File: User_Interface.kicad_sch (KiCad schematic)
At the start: 24 parts, among them SW1 SPST-NO, SW2 SPST-NO, U11 74LVC1G38, U12 74LVC1G38, U13 74LVC1G38

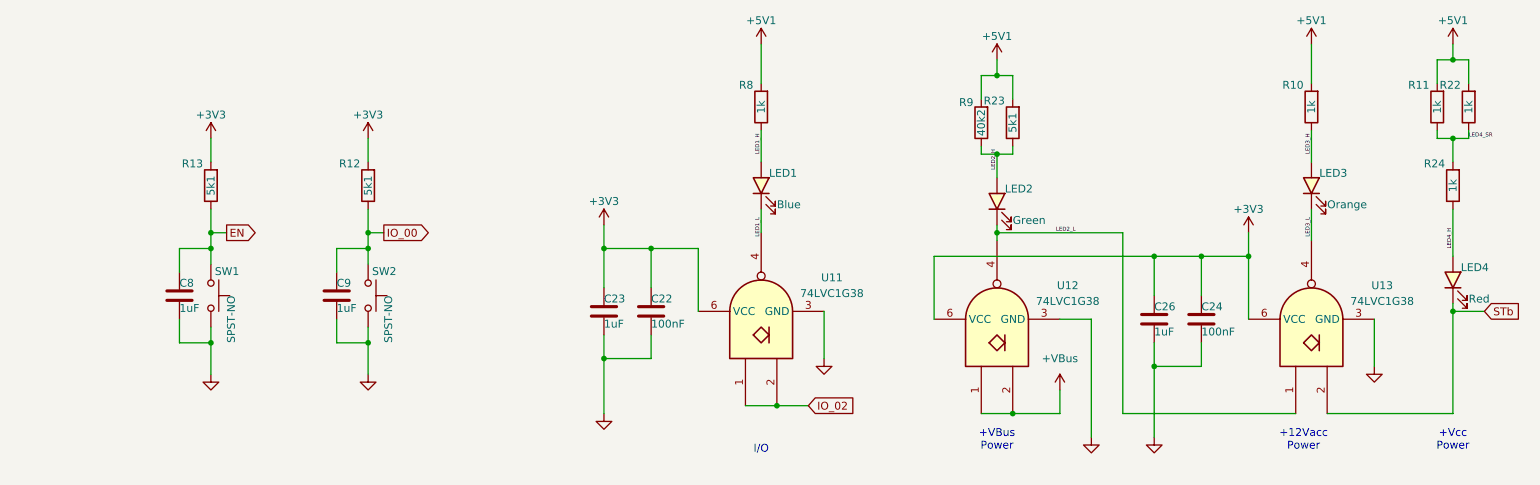
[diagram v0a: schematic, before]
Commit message: streamlined routing by discarding legacy GPIO pinout compatibility. reduced Vin to Vcc and Vbus (no more +16V) includes CAN & Vehicle inputs (need to move to 2nd board, though) added wake-on-start by wiring Vacc to RTC_IO
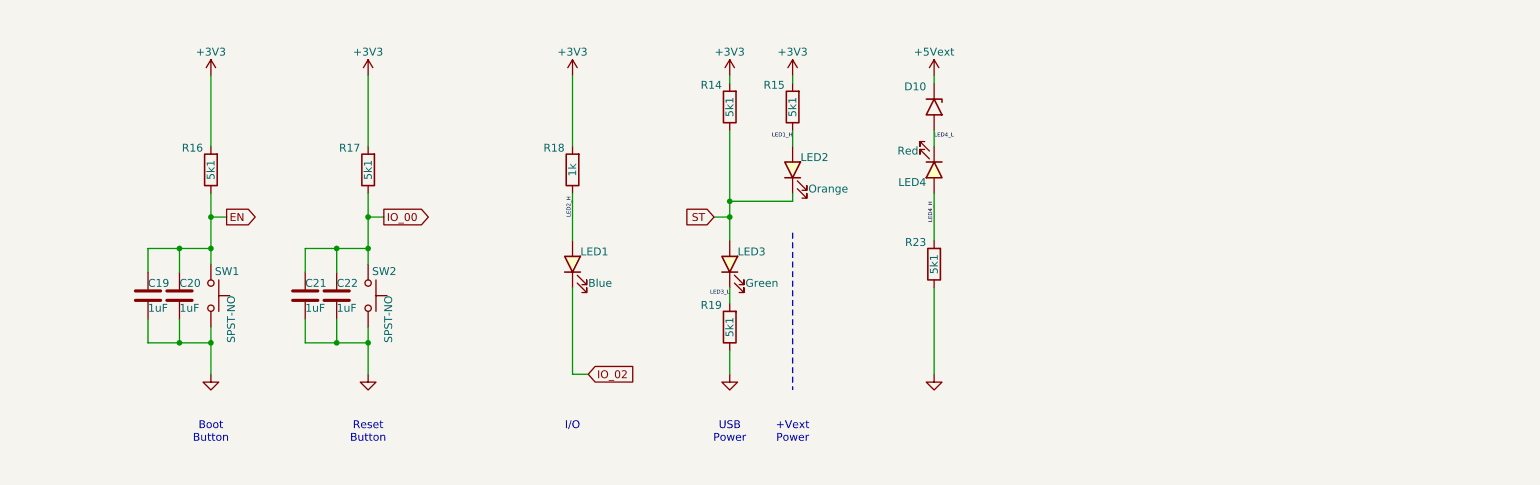
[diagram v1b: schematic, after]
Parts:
- removed C23, C26, C8, C9: 1uF, Capacitors:C0201_Dense, symbol Device:C
- removed C24: 100nF, Capacitors:C0201_Dense, symbol Device:C
- removed LED2: Green, Personal_FootprintLibrary:LED_0201-2, symbol PersonalSchematicSymbolLibrary:LED_Green
- removed R10, R11, R22, R24: 1k, Resistors:R0201_Dense, symbol Device:R
- removed R9: 40k2, Resistors:R0201_Dense, symbol Device:R
- removed U11, U12, U13: 74LVC1G38, Personal_FootprintLibrary:DSF6, symbol 74xGxx:74LVC1G38
- added C19, C20, C21: 1uF, Capacitors:C_0201_Dense, symbol Device:C
- added D10: D15V0H1U2LP-7B, Personal_FootprintLibrary:DFN1006-2, symbol PersonalSchematicSymbolLibrary:TVS_Unidirectional
- added LED4: Red, Personal_FootprintLibrary:LED_0201-2, symbol PersonalSchematicSymbolLibrary:LED_Red
- added R14, R15, R19: 5k1, Resistors:R_0201_Dense, symbol Device:R
- C22: value 100nF -> 1uF; footprint Capacitors:C0201_Dense -> Capacitors:C_0201_Dense; Distributor Link 1 https://www.digikey.com/en/products/detail/murata-electroni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 -> https://www.digikey.com/en/products/detail/samsung-electro-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; Distributor Link 2 https://www.mouser.com/ProductDetail/Murata-Electronics/GRM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 -> https://www.mouser.com/ProductDetail/Samsung-Electro-Mechan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; LCSC C76939 -> C307385; Manufacturer Murata Electronics -> Samsung Electro-Mechanics; Manufacturer Part Number GRM033R61E104KE14D -> CL03A105MO3NRNH
- LED3: renamed from LED4; value Red -> Green; symbol PersonalSchematicSymbolLibrary:LED_Red -> PersonalSchematicSymbolLibrary:LED_Green; Distributor Link 1 https://www.digikey.com/en/products/detail/xinglight/XL-0201SURC/25672952 -> https://www.digikey.com/en/products/detail/xinglight/XL-0201UGC/25673271; LCSC C3646923 -> C3646922; Manufacturer Part Number XL-0201SURC -> XL-0201UGC
- R16: renamed from R13; footprint Resistors:R0201_Dense -> Resistors:R_0201_Dense
- R17: renamed from R12; footprint Resistors:R0201_Dense -> Resistors:R_0201_Dense
- R18: renamed from R8; footprint Resistors:R0201_Dense -> Resistors:R_0201_Dense
- R23: footprint Resistors:R0201_Dense -> Resistors:R_0201_Dense
- renumbered LED3 to LED2
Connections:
- net LED1_L is gone; now on net IO_02: LED1.1 (K)
- net LED3_H is gone; now on net LED1_H: LED2.2 (A)
- net STb is gone; now on net LED3_L: LED3.1 (K)
- net +3V3: now also R18.2, R14.2, R15.2; no longer C22.1
- net EN: now also C19.1, C20.1
- net GND: now also R23.1, C19.2, C20.2, C21.2, R19.1
- net IO_00: now also C22.1, C21.1
- net LED1_H: now also R15.1; no longer LED1.2 (A), R18.1
- net LED2_H: now also LED1.2 (A), R18.1; no longer R23.1
- net LED3_L: now also R19.2; no longer LED2.1 (K)
- net LED4_H: now also R23.2, LED4.2 (A); no longer LED3.2 (A)
- removed net +5V1: R18.2, R23.2
- new net +5Vext: D10.1 (K)
- new net LED4_L: D10.2 (A), LED4.1 (K)
- new net ST: LED2.1 (K), LED3.2 (A), R14.1
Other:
- note added: "+Vext Power"
- note added: "Boot Button"
- note added: "Reset Button"
- note added: "USB Power"
- note removed: "+12Vacc Power"
- note removed: "+VBus Power"
- note removed: "+Vcc Power"
- moved on the sheet: LED1, LED2, LED3, R16, R17, R18

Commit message: Update .gitignore, BOM-ESP32-S3 Pico D1.csv, CANBus_Interface.kicad_sch, and 14 more files
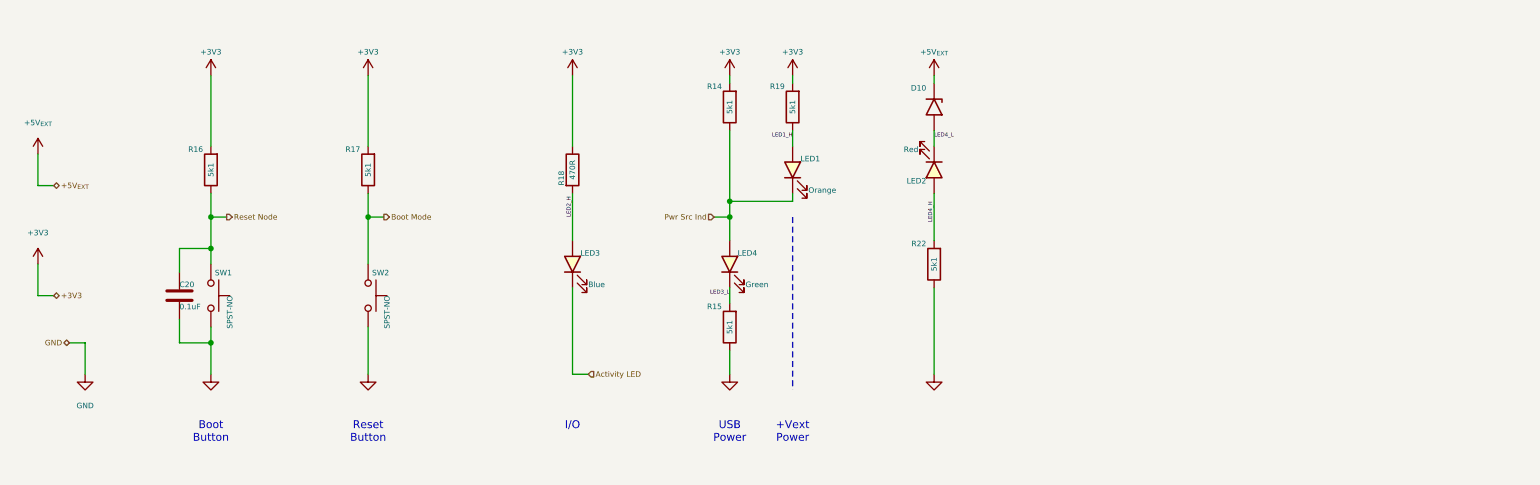
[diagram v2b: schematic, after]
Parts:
- removed C19, C21, C22: 1uF, Capacitors:C_0201_Dense, symbol Device:C
- removed R23: 5k1, Resistors:R_0201_Dense, symbol Device:R
- added R22: 5k1, Resistors:R_0201_Dense, symbol Device:R
- C20: value 1uF -> 0.1uF; Distributor Link 1 https://www.digikey.com/en/products/detail/samsung-electro-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 -> https://www.digikey.com/en/products/detail/murata-electroni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; Distributor Link 2 https://www.mouser.com/ProductDetail/Samsung-Electro-Mechan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 -> https://www.mouser.com/ProductDetail/Murata-Electronics/GRT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; LCSC C307385 -> C915760; Manufacturer Samsung Electro-Mechanics -> Murata Electronics; Manufacturer Part Number CL03A105MO3NRNH -> GRT033R61E104KE01D
- R14, R15, R16, R17, R19: Distributor Link 1 (none) -> https://www.digikey.com/en/products/detail/yageo/AC0201FR-0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; Distributor Link 2 https://www.mouser.com/ProductDetail/Royalohm/0201WMF5101TE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 -> https://www.mouser.com/ProductDetail/YAGEO/AC0201FR-075K1L?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; LCSC C270344 -> C226588; Manufacturer UNI-ROYAL(Uniroyal Elec) -> YAGEO; Manufacturer Part Number 0201WMF5101TEE -> AC0201FR-075K1L
- R18: value 1k -> 470R; Distributor Link 1 (none) -> https://www.digikey.com/en/products/detail/yageo/AC0201FR-0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; Distributor Link 2 https://www.mouser.com/ProductDetail/Royalohm/0201WMF1001TE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 -> https://www.mouser.com/ProductDetail/YAGEO/AC0201FR-07470RL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; LCSC C270365 -> C226558; Manufacturer UNI-ROYAL(Uniroyal Elec) -> YAGEO; Manufacturer Part Number 0201WMF1001TEE -> AC0201FR-07470RL
- renumbered LED2 to LED1, LED4 to LED2, LED1 to LED3, LED3 to LED4
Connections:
- net +3V3: now also R18.1, R19.2; no longer R15.2, R18.2
- net GND: now also R15.1, R22.1; no longer R19.1
- net LED1_H: now also R19.1; no longer R15.1
- net LED2_H: now also R18.2; no longer R18.1
- net LED3_L: now also R15.2; no longer R19.2
- net LED4_H: now also R22.2
- net +5Vext renamed +5V_{EXT}
- net EN renamed Reset Node
- net IO_00 renamed Boot Mode
- net IO_02 renamed Activity LED
- net ST renamed Pwr Src Ind

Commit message: Update CANBus_Interface.kicad_sch, ESP32-S3 D1 Pico Board.kicad_sch, ESP32-S3 Pico D1.kicad_pcb, and 15 more files
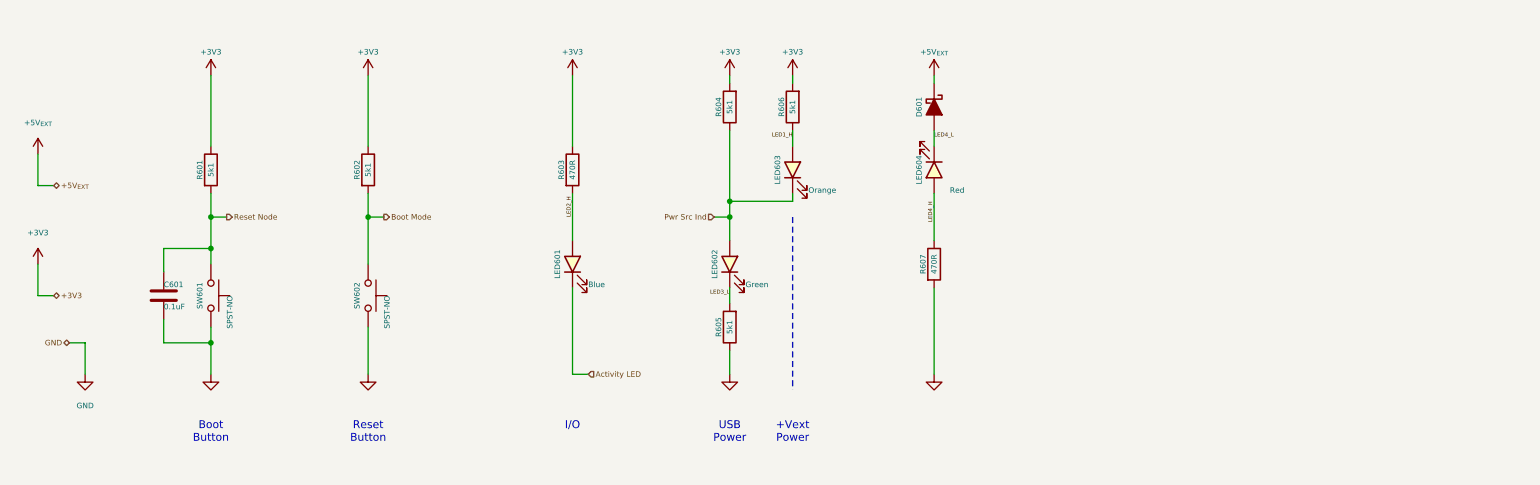
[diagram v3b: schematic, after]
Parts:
- removed D10: D15V0H1U2LP-7B, Personal_FootprintLibrary:DFN1006-2, symbol PersonalSchematicSymbolLibrary:TVS_Unidirectional
- removed R22: 5k1, Resistors:R_0201_Dense, symbol Device:R
- added D601: PMEG4002ESFYL, Personal_FootprintLibrary:DSN0603-2, symbol PersonalSchematicSymbolLibrary:D_Schottky_Filled
- added R607: 470R, My Resistors:R_0201_Dense, symbol Device:R
- C601: renamed from C20; footprint Capacitors:C_0201_Dense -> My Capacitors:C_0201_Dense
- R601: renamed from R16; footprint Resistors:R_0201_Dense -> My Resistors:R_0201_Dense
- R602: renamed from R17; footprint Resistors:R_0201_Dense -> My Resistors:R_0201_Dense
- R603: renamed from R18; footprint Resistors:R_0201_Dense -> My Resistors:R_0201_Dense
- R604: renamed from R14; footprint Resistors:R_0201_Dense -> My Resistors:R_0201_Dense
- R605: renamed from R15; footprint Resistors:R_0201_Dense -> My Resistors:R_0201_Dense
- R606: renamed from R19; footprint Resistors:R_0201_Dense -> My Resistors:R_0201_Dense
- renumbered LED3 to LED601, LED4 to LED602, LED1 to LED603, LED2 to LED604, SW1 to SW601, SW2 to SW602
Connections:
- net +3V3: now also R601.1, R602.1; no longer R601.2, R602.2
- net +5V_{EXT}: now also D601.1 (K)
- net Boot Mode: now also R602.2; no longer R602.1
- net GND: now also R607.2
- net LED4_H: now also R607.1
- net LED4_L: now also D601.2 (A)
- net Reset Node: now also R601.2; no longer R601.1
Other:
- moved on the sheet: C601, R601, R602

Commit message: Update CAN_Interface.kicad_sch, ESP32-S3 D1 Pico Board.kicad_sch, ESP32-S3 Pico D1.kicad_pcb, and 5 more files
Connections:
- net Reset Node renamed ~{Reset Node}
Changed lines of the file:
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@@
 		)
 	)
-	(hierarchical_label "Reset Node"
+	(hierarchical_label "~{Reset Node}"
 		(shape output)
 		(at 68.58 91.44 0)

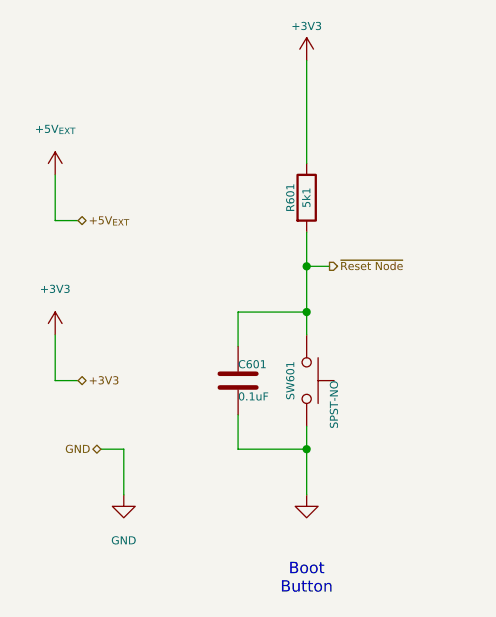
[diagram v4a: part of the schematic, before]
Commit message: fixed hierarchical sheets; replaced pin headers with ESP32-S3_D1_Pico symbol
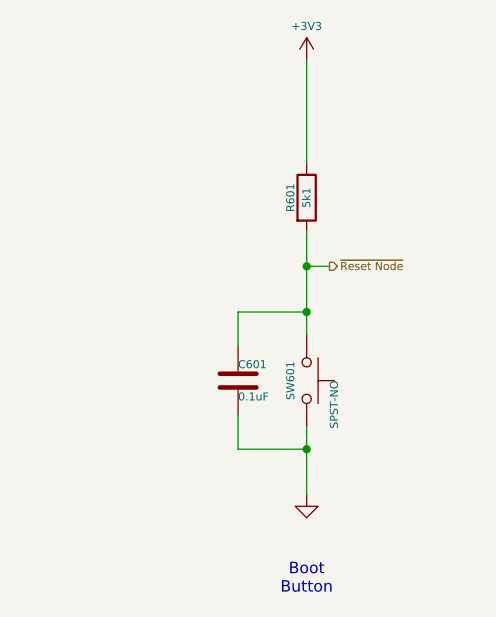
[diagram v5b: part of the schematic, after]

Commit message: Update ESP32-S3 Pico D1-Main.kicad_sch, ESP32-S3 Pico D1.kicad_pcb, ESP32-S3 Pico D1.kicad_prl, and 7 more files
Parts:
- added +V601, +V602, +V603, +V604, +V605, +V608: +3V3, symbol My Power Management:+V (Local)
- added +V606, +V607: +5V_{EXT}, symbol My Power Management:+V (Local)
- added GND601, GND602, GND603, GND604, GND605: GND, symbol My Power Management:GND (Local)
- D601: footprint Personal_FootprintLibrary:DSN0603-2 -> My Package_Leadless:DFN0603-2
- R601, R602, R603, R604, R605, R606, R607: footprint My Resistors:R_0201_Dense -> My Resistors:R_0201_Nominal
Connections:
- net +3V3: now also +V601.1, +V602.1, +V603.1, +V604.1, +V605.1, +V608.1
- net +5V_{EXT}: now also +V606.1, +V607.1
- net GND: now also GND601.1 (GND), GND602.1 (GND), GND603.1 (GND), GND604.1 (GND), GND605.1 (GND)
